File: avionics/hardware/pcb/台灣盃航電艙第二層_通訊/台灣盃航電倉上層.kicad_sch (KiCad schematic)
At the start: 38 parts, among them J1 SMA, J2 SMA, U1 LIS3MDL, U2 NEO-M9N, U3 E22-900T22S, U4 Connector

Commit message: 上傳新的連接器
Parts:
- U4: footprint Connector_PinHeader_1.00mm:PinHeader_2x17_P1.00mm_Vertical -> Connector_PinHeader_2.54mm:PinHeader_2x20_P2.54mm_Vertical
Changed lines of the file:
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@@
 			)
 		)
-		(property "Footprint" "Connector_PinHeader_1.00mm:PinHeader_2x17_P1.00mm_Vertical"
+		(property "Footprint" "Connector_PinHeader_2.54mm:PinHeader_2x20_P2.54mm_Vertical"
 			(at 226.06 85.09 0)
 			(effects

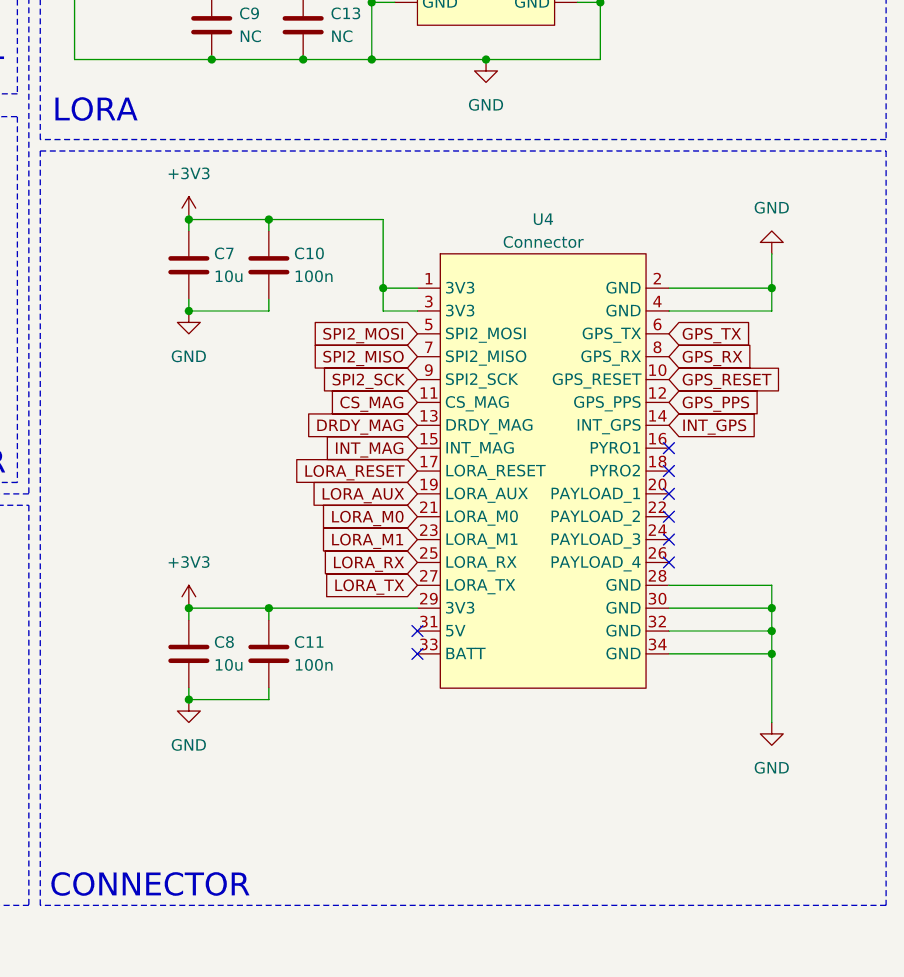
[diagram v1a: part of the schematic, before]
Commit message: 將第一至三層連接器修改成PC104規格，第四層還未進行
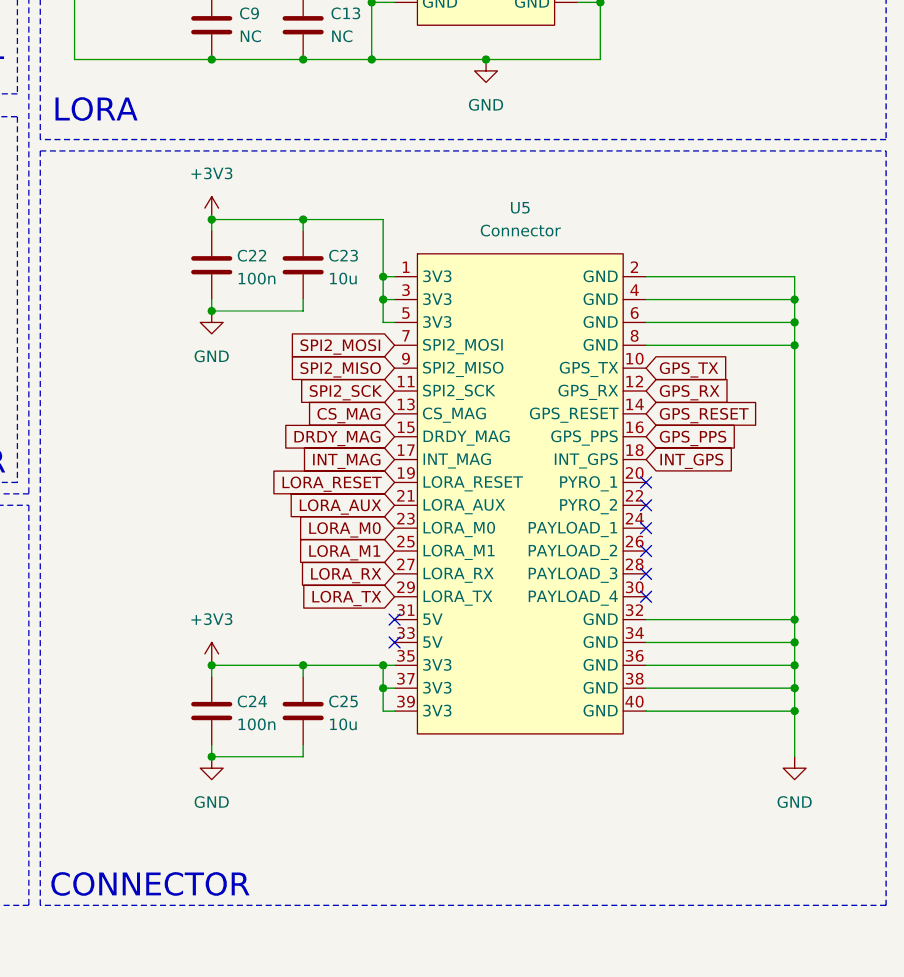
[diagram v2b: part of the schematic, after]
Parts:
- removed C10, C11: 100n, Capacitor_SMD:C_0603_1608Metric, symbol Device:C
- removed C7, C8: 10u, Capacitor_SMD:C_0805_2012Metric, symbol Device:C
- removed U4: Connector, Connector_PinHeader_2.54mm:PinHeader_2x20_P2.54mm_Vertical, symbol MySymbol:2x16排針母座連接
- added C22, C24: 100n, Capacitor_SMD:C_0402_1005Metric, symbol Device:C
- added C23, C25: 10u, Capacitor_SMD:C_0603_1608Metric, symbol Device:C
- added U5: Connector, Connector_PinHeader_2.54mm:PinHeader_2x20_P2.54mm_Vertical, symbol MySymbol:2*20 PC104
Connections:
- net +3V3: now also C22.1, C23.1, C24.1, C25.1, U5.1 (3V3), U5.3 (3V3), U5.35 (3V3), U5.37 (3V3), U5.39 (3V3), U5.5 (3V3)
- net CS_MAG: now also U5.13 (CS_MAG)
- net DRDY_MAG: now also U5.15 (DRDY_MAG)
- net GND: now also C22.2, C23.2, C24.2, C25.2, U5.2 (GND), U5.32 (GND), U5.34 (GND), U5.36 (GND), U5.38 (GND), U5.4 (GND), U5.40 (GND), U5.6 (GND), U5.8 (GND)
- net GPS_PPS: now also U5.16 (GPS_PPS)
- net GPS_RESET: now also U5.14 (GPS_RESET)
- net GPS_RX: now also U5.12 (GPS_RX)
- net GPS_TX: now also U5.10 (GPS_TX)
- net INT_GPS: now also U5.18 (INT_GPS)
- net INT_MAG: now also U5.17 (INT_MAG)
- net LORA_AUX: now also U5.21 (LORA_AUX)
- net LORA_M0: now also U5.23 (LORA_M0)
- net LORA_M1: now also U5.25 (LORA_M1)
- net LORA_RESET: now also U5.19 (LORA_RESET)
- net LORA_RX: now also U5.27 (LORA_RX)
- net LORA_TX: now also U5.29 (LORA_TX)
- net SPI2_MISO: now also U5.9 (SPI2_MISO)
- net SPI2_MOSI: now also U5.7 (SPI2_MOSI)
- net SPI2_SCK: now also U5.11 (SPI2_SCK)
